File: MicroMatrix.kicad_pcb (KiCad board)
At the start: 2 copper layers, 20 x 20 mm, 70 parts

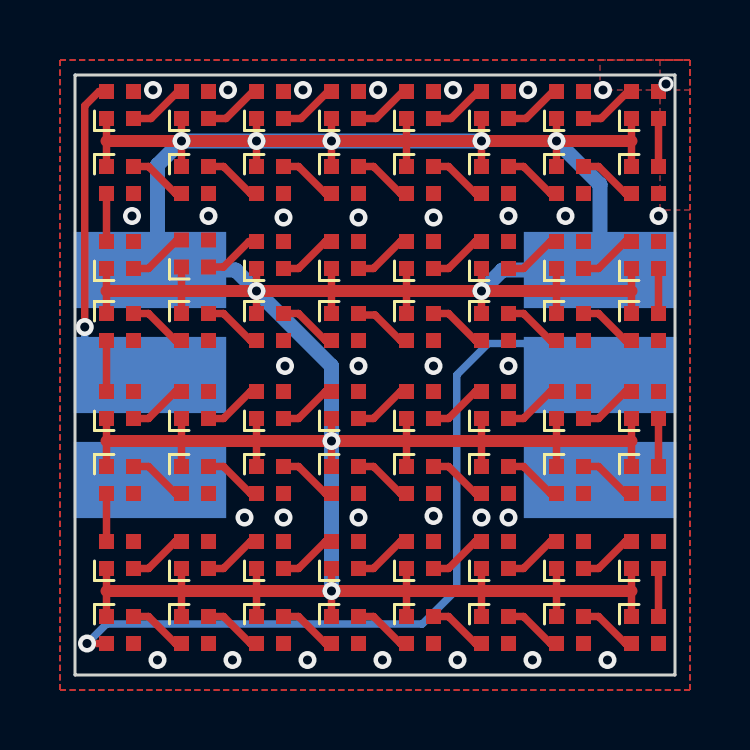
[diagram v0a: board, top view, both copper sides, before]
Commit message: Fixed the 3rd row postion (0.1mm)
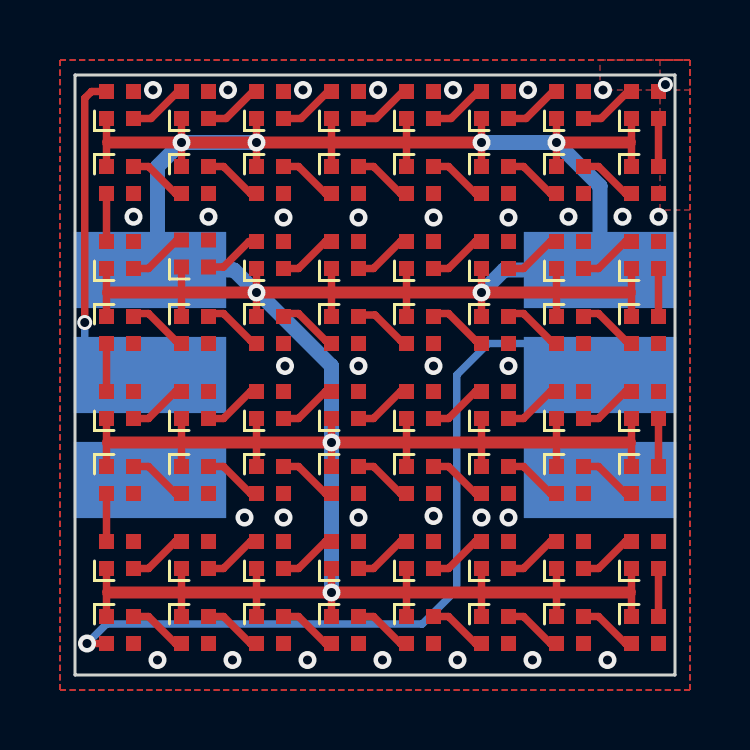
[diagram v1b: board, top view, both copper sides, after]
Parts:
- moved D25 0.10 mm to (149.0, 97.5)
- moved D26 0.10 mm to (146.5, 97.5)
- moved D27 0.10 mm to (144.0, 97.5)
- moved D28 0.10 mm to (141.5, 97.5)
- moved D29 0.10 mm to (139.0, 97.5)
- moved D30 0.10 mm to (136.5, 97.5)
- moved D31 0.10 mm to (134.0, 97.5)
- moved D32 0.10 mm to (131.5, 97.5)
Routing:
- net +5V: track 159.2 -> 151.3 mm, vias 9 -> 8
- net GND: vias 33 -> 34
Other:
- board text added: "REV1.2"
- board text removed: "REV1.1"

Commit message: Updated Panel PCB to REV1.2
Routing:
- net +5V: track 151.3 -> 153.9 mm
- net DIN: track 14.0 -> 15.2 mm
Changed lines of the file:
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@@
   (segment (start 132.533193 90.45) (end 133.433193 89.55) (width 0.25) (layer "F.Cu") (net 1))
   (segment (start 131.95 90.45) (end 132.533193 90.45) (width 0.25) (layer "F.Cu") (net 1))
-  (segment (start 147.6 89.5) (end 147.6 89.4) (width 0.25) (layer "F.Cu") (net 2))
   (via (at 134.45 93.725) (size 0.6) (drill 0.3) (layers "F.Cu" "B.Cu") (free) (net 2))
   (via (at 142.75 108.5) (size 0.6) (drill 0.3) (layers "F.Cu" "B.Cu") (free) (net 2))
@@
   (segment (start 131.05 89.55) (end 130.55 89.55) (width 0.25) (layer "F.Cu") (net 3))
   (via (at 130.325 97.25) (size 0.5) (drill 0.3) (layers "F.Cu" "B.Cu") (free) (net 3))
+  (segment (start 130.325 97.25) (end 130.325 98.075) (width 0.25) (layer "B.Cu") (net 3))
   (segment (start 131.125 99) (end 130.325 98.2) (width 0.25) (layer "B.Cu") (net 3))
+  (segment (start 130.325 98.075) (end 131.75 99.5) (width 0.25) (layer "B.Cu") (net 3))
   (segment (start 132.5 99) (end 130.95 99) (width 0.25) (layer "B.Cu") (net 3))
-  (segment (start 130.325 98.05) (end 130.325 97.25) (width 0.25) (layer "B.Cu") (net 3))
-  (segment (start 130.95 99) (end 130.35 98.4) (width 0.25) (layer "B.Cu") (net 3))
   (segment (start 132.5 99) (end 131.125 99) (width 0.25) (layer "B.Cu") (net 3))
   (segment (start 148.55 101.2) (end 148.55 102.05) (width 0.25) (layer "F.Cu") (net 4))
@@
   (segment (start 143.55 90.45) (end 143.55 92.05) (width 0.25) (layer "F.Cu") (net 4))
   (segment (start 131.05 96.2) (end 131.05 96.95) (width 0.25) (layer "F.Cu") (net 4))
+  (segment (start 131.05 91.25) (end 148.55 91.25) (width 0.4) (layer "F.Cu") (net 4))
   (segment (start 131.05 105.45) (end 131.05 106.2) (width 0.25) (layer "F.Cu") (net 4))
   (segment (start 133.55 107.05) (end 133.55 105.45) (width 0.25) (layer "F.Cu") (net 4))
@@
   (segment (start 131.1 101.25) (end 148.5 101.25) (width 0.4) (layer "F.Cu") (net 4))
   (segment (start 148.55 95.45) (end 148.55 96.2) (width 0.25) (layer "F.Cu") (net 4))
-  (segment (start 146.05 91.25) (end 148.5 91.25) (width 0.4) (layer "F.Cu") (net 4))
   (segment (start 148.55 96.2) (end 148.55 96.95) (width 0.25) (layer "F.Cu") (net 4))
   (segment (start 143.55 96.25) (end 143.55 96.95) (width 0.25) (layer "F.Cu") (net 4))
@@
   (segment (start 148.55 107.05) (end 148.55 106.2) (width 0.25) (layer "F.Cu") (net 4))
   (segment (start 148.55 90.45) (end 148.55 91.2) (width 0.25) (layer "F.Cu") (net 4))
-  (segment (start 131.1 91.25) (end 143.55 91.25) (width 0.4) (layer "F.Cu") (net 4))
   (segment (start 133.55 91.25) (end 133.55 92.05) (width 0.25) (layer "F.Cu") (net 4))
   (segment (start 143.55 105.45) (end 143.55 107.05) (width 0.25) (layer "F.Cu") (net 4))
@@
   (via (at 138.55 106.25) (size 0.6) (drill 0.3) (layers "F.Cu" "B.Cu") (net 4))
   (via (at 146.05 91.25) (size 0.6) (drill 0.3) (layers "F.Cu" "B.Cu") (net 4))
+  (segment (start 146.05 91.25) (end 143.55 91.25) (width 0.5) (layer "B.Cu") (net 4))
   (segment (start 138.55 101.25) (end 138.55 106.25) (width 0.5) (layer "B.Cu") (net 4))
   (segment (start 144.3 95.5) (end 147.5 95.5) (width 0.5) (layer "B.Cu") (net 4))
@@
   (segment (start 133.55 91.25) (end 132.75 92.05) (width 0.5) (layer "B.Cu") (net 4))
   (segment (start 135.3 95.5) (end 132.5 95.5) (width 0.5) (layer "B.Cu") (net 4))
-  (segment (start 143.55 91.25) (end 146.05 91.25) (width 0.5) (layer "B.Cu") (net 4))
   (segment (start 136.05 96.25) (end 135.3 95.5) (width 0.5) (layer "B.Cu") (net 4))
   (segment (start 132.75 95.25) (end 132.5 95.5) (width 0.25) (layer "B.Cu") (net 4))

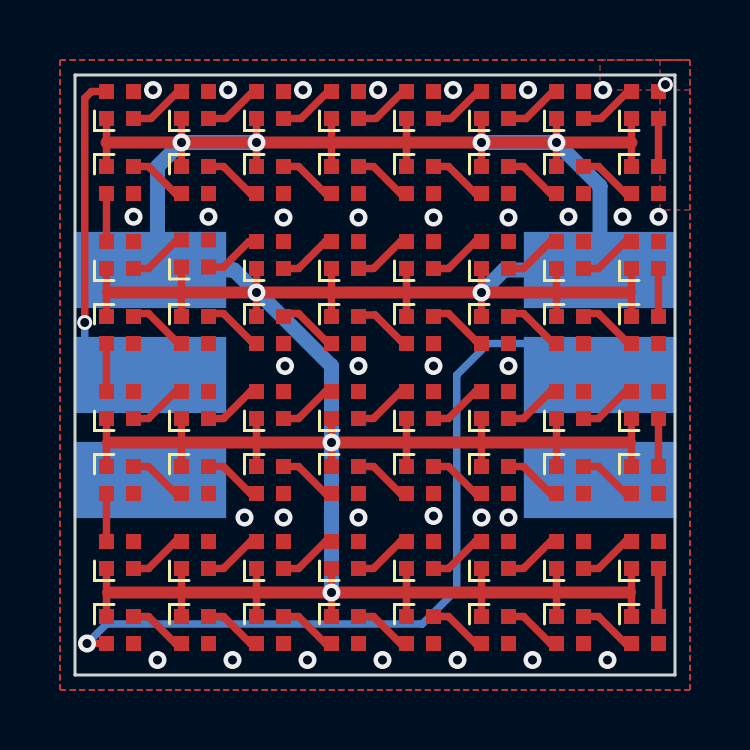
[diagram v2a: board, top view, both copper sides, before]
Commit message: Fixed Trace in REV1.2
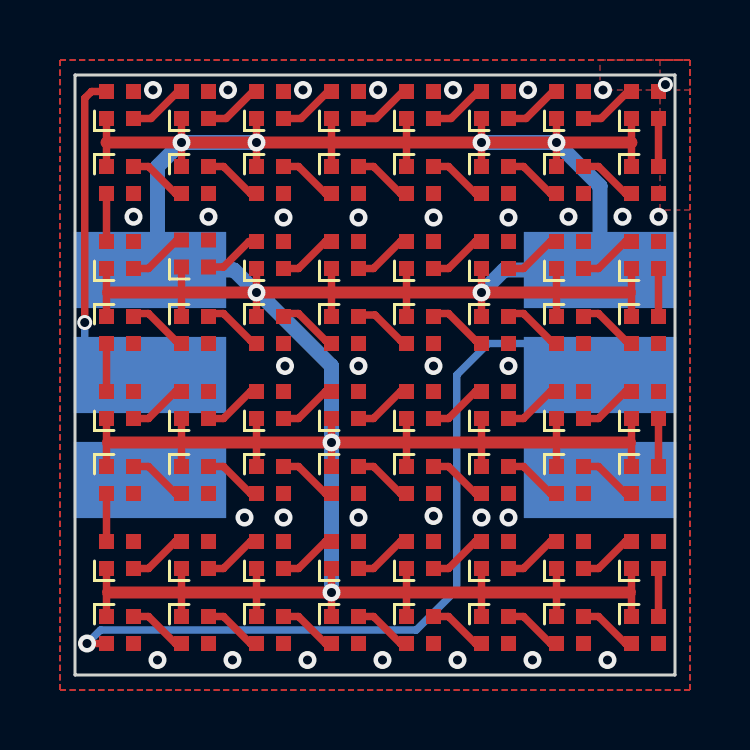
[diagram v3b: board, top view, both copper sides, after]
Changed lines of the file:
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@@
   (segment (start 130.4 107.95) (end 131.05 107.95) (width 0.25) (layer "F.Cu") (net 67))
   (via (at 130.4 107.95) (size 0.6) (drill 0.3) (layers "F.Cu" "B.Cu") (free) (net 67))
+  (segment (start 142.725 99) (end 142.725 106.15) (width 0.25) (layer "B.Cu") (net 67))
   (segment (start 143.775 97.95) (end 142.725 99) (width 0.25) (layer "B.Cu") (net 67))
-  (segment (start 131.05 107.3) (end 130.4 107.95) (width 0.25) (layer "B.Cu") (net 67))
-  (segment (start 142.725 99) (end 142.725 106.15) (width 0.25) (layer "B.Cu") (net 67))
-  (segment (start 141.575 107.3) (end 131.05 107.3) (width 0.25) (layer "B.Cu") (net 67))
-  (segment (start 146.45 97.95) (end 147.5 99) (width 0.25) (layer "B.Cu") (net 67))
-  (segment (start 142.725 106.15) (end 141.575 107.3) (width 0.25) (layer "B.Cu") (net 67))
-  (segment (start 143.775 97.95) (end 146.45 97.95) (width 0.25) (layer "B.Cu") (net 67))
+  (segment (start 130.85 107.5) (end 130.4 107.95) (width 0.25) (layer "B.Cu") (net 67))
+  (segment (start 147.5 99) (end 146.45 97.95) (width 0.25) (layer "B.Cu") (net 67))
+  (segment (start 146.45 97.95) (end 143.775 97.95) (width 0.25) (layer "B.Cu") (net 67))
+  (segment (start 141.375 107.5) (end 130.85 107.5) (width 0.25) (layer "B.Cu") (net 67))
+  (segment (start 142.725 106.15) (end 141.375 107.5) (width 0.25) (layer "B.Cu") (net 67))
   (zone locked (net 2) (net_name "GND") (layers F&B.Cu) (hatch edge 0.508)
     (connect_pads (clearance 0.128))

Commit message: Updated PCB to REV1.3 Replaced SK6805 footprint/symbol with a own version
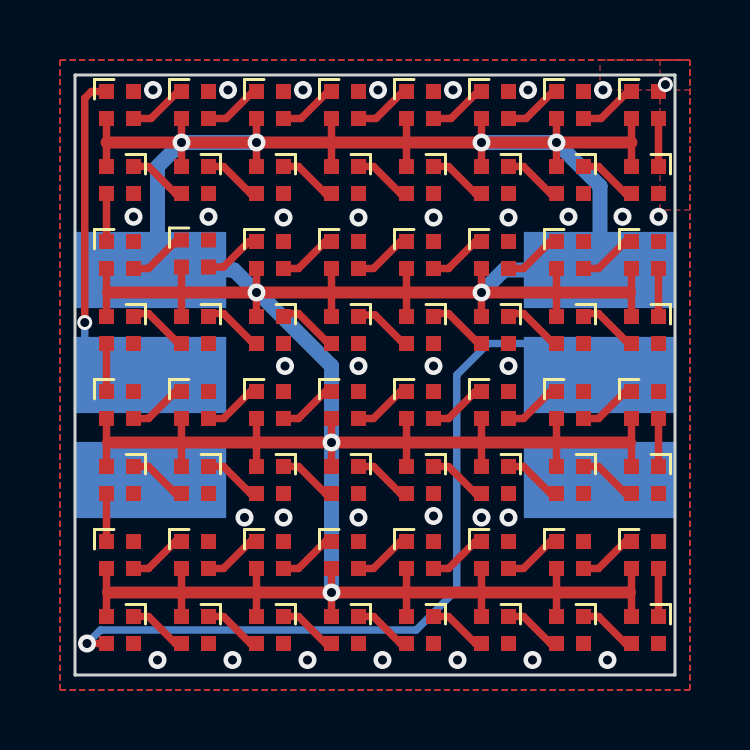
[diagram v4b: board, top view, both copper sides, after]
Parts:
- D1, D10, D11, D12, D13, D14, D15, D16, D17, D18, D19, D2, D20, D21, D22, D23, D24, D25, D26, D27, D28, D29, D3, D30, D31, D32, D33, D34, D35, D36, D37, D38, D39, D4, D40, D41, D42, D43, D44, D45, D46, D47, D48, D49, D5, D50, D51, D52, D53, D54, D55, D56, D57, D58, D59, D6, D60, D61, D62, D63, D64, D7, D8, D9: footprint LED_SMD:LED_SK6812_EC15_1.5x1.5mm -> SK6805-EC15:SK6805-EC15
- turned D1 to 0 degrees
- turned D10 to -90 degrees
- turned D11 to -90 degrees
- turned D12 to -90 degrees
- turned D13 to -90 degrees
- turned D14 to -90 degrees
- turned D15 to -90 degrees
- turned D16 to -90 degrees
- turned D17 to 0 degrees
- turned D18 to 0 degrees
- turned D19 to 0 degrees
- turned D2 to 0 degrees
- turned D20 to 0 degrees
- turned D21 to 0 degrees
- turned D22 to 0 degrees
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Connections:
- D1 pad 1: Net-(D1-Pad1) -> DIN
- D1 pad 2: GND -> +5V
- D1 pad 3: DIN -> Net-(D1-DOUT)
- D1 pad 4: +5V -> GND
- D10 pad 1: Net-(D10-Pad1) -> Net-(D10-DIN)
- D10 pad 2: GND -> +5V
- D10 pad 3: Net-(D10-Pad3) -> Net-(D10-DOUT)
- D10 pad 4: +5V -> GND
- D11 pad 1: Net-(D11-Pad1) -> Net-(D10-DOUT)
- D11 pad 2: GND -> +5V
- D11 pad 3: Net-(D10-Pad1) -> Net-(D11-DOUT)
- D11 pad 4: +5V -> GND
- D12 pad 1: Net-(D12-Pad1) -> Net-(D11-DOUT)
- D12 pad 2: GND -> +5V
- D12 pad 3: Net-(D11-Pad1) -> Net-(D12-DOUT)
- D12 pad 4: +5V -> GND
- D13 pad 1: Net-(D13-Pad1) -> Net-(D12-DOUT)
- D13 pad 2: GND -> +5V
- D13 pad 3: Net-(D12-Pad1) -> Net-(D13-DOUT)
- D13 pad 4: +5V -> GND
- D14 pad 1: Net-(D14-Pad1) -> Net-(D13-DOUT)
- D14 pad 2: GND -> +5V
- D14 pad 3: Net-(D13-Pad1) -> Net-(D14-DOUT)
- D14 pad 4: +5V -> GND
- D15 pad 1: Net-(D15-Pad1) -> Net-(D14-DOUT)
- D15 pad 2: GND -> +5V
- D15 pad 3: Net-(D14-Pad1) -> Net-(D15-DOUT)
- D15 pad 4: +5V -> GND
- D16 pad 1: Net-(D16-Pad1) -> Net-(D15-DOUT)
- D16 pad 2: GND -> +5V
- D16 pad 3: Net-(D15-Pad1) -> Net-(D16-DOUT)
- D16 pad 4: +5V -> GND
- D17 pad 1: Net-(D17-Pad1) -> Net-(D16-DOUT)
- D17 pad 2: GND -> +5V
- D17 pad 3: Net-(D16-Pad1) -> Net-(D17-DOUT)
- D17 pad 4: +5V -> GND
- D18 pad 1: Net-(D18-Pad1) -> Net-(D17-DOUT)
- D18 pad 2: GND -> +5V
- D18 pad 3: Net-(D17-Pad1) -> Net-(D18-DOUT)
- D18 pad 4: +5V -> GND
- D19 pad 1: Net-(D19-Pad1) -> Net-(D18-DOUT)
- D19 pad 2: GND -> +5V
- D19 pad 3: Net-(D18-Pad1) -> Net-(D19-DOUT)
- D19 pad 4: +5V -> GND
- D2 pad 1: Net-(D2-Pad1) -> Net-(D1-DOUT)
- D2 pad 2: GND -> +5V
- D2 pad 3: Net-(D1-Pad1) -> Net-(D2-DOUT)
- D2 pad 4: +5V -> GND
- D20 pad 1: Net-(D20-Pad1) -> Net-(D19-DOUT)
- D20 pad 2: GND -> +5V
- D20 pad 3: Net-(D19-Pad1) -> Net-(D20-DOUT)
- D20 pad 4: +5V -> GND
- D21 pad 1: Net-(D21-Pad1) -> Net-(D20-DOUT)
- D21 pad 2: GND -> +5V
- D21 pad 3: Net-(D20-Pad1) -> Net-(D21-DOUT)
- D21 pad 4: +5V -> GND
- D22 pad 1: Net-(D22-Pad1) -> Net-(D21-DOUT)
- D22 pad 2: GND -> +5V
- D22 pad 3: Net-(D21-Pad1) -> Net-(D22-DOUT)
- D22 pad 4: +5V -> GND
- D23 pad 1: Net-(D23-Pad1) -> Net-(D22-DOUT)
- D23 pad 2: GND -> +5V
- D23 pad 3: Net-(D22-Pad1) -> Net-(D23-DOUT)
- D23 pad 4: +5V -> GND
- D24 pad 1: Net-(D24-Pad1) -> Net-(D23-DOUT)
- D24 pad 2: GND -> +5V
- D24 pad 3: Net-(D23-Pad1) -> Net-(D24-DOUT)
- D24 pad 4: +5V -> GND
- D25 pad 1: Net-(D25-Pad1) -> Net-(D24-DOUT)
- D25 pad 2: GND -> +5V
- D25 pad 3: Net-(D24-Pad1) -> Net-(D25-DOUT)
- D25 pad 4: +5V -> GND
- D26 pad 1: Net-(D26-Pad1) -> Net-(D25-DOUT)
- D26 pad 2: GND -> +5V
- D26 pad 3: Net-(D25-Pad1) -> Net-(D26-DOUT)
- D26 pad 4: +5V -> GND
- D27 pad 1: Net-(D27-Pad1) -> Net-(D26-DOUT)
- D27 pad 2: GND -> +5V
- D27 pad 3: Net-(D26-Pad1) -> Net-(D27-DOUT)
- D27 pad 4: +5V -> GND
- D28 pad 1: Net-(D28-Pad1) -> Net-(D27-DOUT)
- D28 pad 2: GND -> +5V
- D28 pad 3: Net-(D27-Pad1) -> Net-(D28-DOUT)
- D28 pad 4: +5V -> GND
- D29 pad 1: Net-(D29-Pad1) -> Net-(D28-DOUT)
- D29 pad 2: GND -> +5V
- D29 pad 3: Net-(D28-Pad1) -> Net-(D29-DOUT)
- D29 pad 4: +5V -> GND
- D3 pad 1: Net-(D3-Pad1) -> Net-(D2-DOUT)
- D3 pad 2: GND -> +5V
- D3 pad 3: Net-(D2-Pad1) -> Net-(D3-DOUT)
- D3 pad 4: +5V -> GND
- D30 pad 1: Net-(D30-Pad1) -> Net-(D29-DOUT)
- D30 pad 2: GND -> +5V
- D30 pad 3: Net-(D29-Pad1) -> Net-(D30-DOUT)
- D30 pad 4: +5V -> GND
- D31 pad 1: Net-(D31-Pad1) -> Net-(D30-DOUT)
- D31 pad 2: GND -> +5V
- D31 pad 3: Net-(D30-Pad1) -> Net-(D31-DOUT)
- D31 pad 4: +5V -> GND
- D32 pad 1: Net-(D32-Pad1) -> Net-(D31-DOUT)
- D32 pad 2: GND -> +5V
- D32 pad 3: Net-(D31-Pad1) -> Net-(D32-DOUT)
- D32 pad 4: +5V -> GND
- D33 pad 1: Net-(D33-Pad1) -> Net-(D32-DOUT)
- D33 pad 2: GND -> +5V
- D33 pad 3: Net-(D32-Pad1) -> Net-(D33-DOUT)
- D33 pad 4: +5V -> GND
- D34 pad 1: Net-(D34-Pad1) -> Net-(D33-DOUT)
- D34 pad 2: GND -> +5V
- D34 pad 3: Net-(D33-Pad1) -> Net-(D34-DOUT)
- D34 pad 4: +5V -> GND
- D35 pad 1: Net-(D35-Pad1) -> Net-(D34-DOUT)
- D35 pad 2: GND -> +5V
- D35 pad 3: Net-(D34-Pad1) -> Net-(D35-DOUT)
- D35 pad 4: +5V -> GND
- D36 pad 1: Net-(D36-Pad1) -> Net-(D35-DOUT)
- D36 pad 2: GND -> +5V
- D36 pad 3: Net-(D35-Pad1) -> Net-(D36-DOUT)
- D36 pad 4: +5V -> GND
- D37 pad 1: Net-(D37-Pad1) -> Net-(D36-DOUT)
- D37 pad 2: GND -> +5V
- D37 pad 3: Net-(D36-Pad1) -> Net-(D37-DOUT)
- D37 pad 4: +5V -> GND
- D38 pad 1: Net-(D38-Pad1) -> Net-(D37-DOUT)
- D38 pad 2: GND -> +5V
- D38 pad 3: Net-(D37-Pad1) -> Net-(D38-DOUT)
- D38 pad 4: +5V -> GND
- D39 pad 1: Net-(D39-Pad1) -> Net-(D38-DOUT)
- D39 pad 2: GND -> +5V
- D39 pad 3: Net-(D38-Pad1) -> Net-(D39-DOUT)
- D39 pad 4: +5V -> GND
- D4 pad 1: Net-(D4-Pad1) -> Net-(D3-DOUT)
- D4 pad 2: GND -> +5V
- D4 pad 3: Net-(D3-Pad1) -> Net-(D4-DOUT)
- D4 pad 4: +5V -> GND
- D40 pad 1: Net-(D40-Pad1) -> Net-(D39-DOUT)
- D40 pad 2: GND -> +5V
- D40 pad 3: Net-(D39-Pad1) -> Net-(D40-DOUT)
- D40 pad 4: +5V -> GND
- D41 pad 1: Net-(D41-Pad1) -> Net-(D40-DOUT)
- D41 pad 2: GND -> +5V
- D41 pad 3: Net-(D40-Pad1) -> Net-(D41-DOUT)
- D41 pad 4: +5V -> GND
- D42 pad 1: Net-(D42-Pad1) -> Net-(D41-DOUT)
- D42 pad 2: GND -> +5V
- D42 pad 3: Net-(D41-Pad1) -> Net-(D42-DOUT)
- D42 pad 4: +5V -> GND
- D43 pad 1: Net-(D43-Pad1) -> Net-(D42-DOUT)
- D43 pad 2: GND -> +5V
- D43 pad 3: Net-(D42-Pad1) -> Net-(D43-DOUT)
- D43 pad 4: +5V -> GND
- D44 pad 1: Net-(D44-Pad1) -> Net-(D43-DOUT)
- D44 pad 2: GND -> +5V
- D44 pad 3: Net-(D43-Pad1) -> Net-(D44-DOUT)
- D44 pad 4: +5V -> GND
- D45 pad 1: Net-(D45-Pad1) -> Net-(D44-DOUT)
- D45 pad 2: GND -> +5V
- D45 pad 3: Net-(D44-Pad1) -> Net-(D45-DOUT)
- D45 pad 4: +5V -> GND
- D46 pad 1: Net-(D46-Pad1) -> Net-(D45-DOUT)
- D46 pad 2: GND -> +5V
- D46 pad 3: Net-(D45-Pad1) -> Net-(D46-DOUT)
- D46 pad 4: +5V -> GND
- D47 pad 1: Net-(D47-Pad1) -> Net-(D46-DOUT)
- D47 pad 2: GND -> +5V
- D47 pad 3: Net-(D46-Pad1) -> Net-(D47-DOUT)
- D47 pad 4: +5V -> GND
- D48 pad 1: Net-(D48-Pad1) -> Net-(D47-DOUT)
- D48 pad 2: GND -> +5V
- D48 pad 3: Net-(D47-Pad1) -> Net-(D48-DOUT)
- D48 pad 4: +5V -> GND
- D49 pad 1: Net-(D49-Pad1) -> Net-(D48-DOUT)
- D49 pad 2: GND -> +5V
- D49 pad 3: Net-(D48-Pad1) -> Net-(D49-DOUT)
- D49 pad 4: +5V -> GND
- D5 pad 1: Net-(D5-Pad1) -> Net-(D4-DOUT)
- D5 pad 2: GND -> +5V
- D5 pad 3: Net-(D4-Pad1) -> Net-(D5-DOUT)
- D5 pad 4: +5V -> GND
- D50 pad 1: Net-(D50-Pad1) -> Net-(D49-DOUT)
- D50 pad 2: GND -> +5V
- D50 pad 3: Net-(D49-Pad1) -> Net-(D50-DOUT)
- D50 pad 4: +5V -> GND
- D51 pad 1: Net-(D51-Pad1) -> Net-(D50-DOUT)
- D51 pad 2: GND -> +5V
- D51 pad 3: Net-(D50-Pad1) -> Net-(D51-DOUT)
- D51 pad 4: +5V -> GND
- D52 pad 1: Net-(D52-Pad1) -> Net-(D51-DOUT)
- D52 pad 2: GND -> +5V
- D52 pad 3: Net-(D51-Pad1) -> Net-(D52-DOUT)
- D52 pad 4: +5V -> GND
- D53 pad 1: Net-(D53-Pad1) -> Net-(D52-DOUT)
- D53 pad 2: GND -> +5V
- D53 pad 3: Net-(D52-Pad1) -> Net-(D53-DOUT)
- D53 pad 4: +5V -> GND
- D54 pad 1: Net-(D54-Pad1) -> Net-(D53-DOUT)
- D54 pad 2: GND -> +5V
- D54 pad 3: Net-(D53-Pad1) -> Net-(D54-DOUT)
- D54 pad 4: +5V -> GND
- D55 pad 1: Net-(D55-Pad1) -> Net-(D54-DOUT)
- D55 pad 2: GND -> +5V
- D55 pad 3: Net-(D54-Pad1) -> Net-(D55-DOUT)
- D55 pad 4: +5V -> GND
- D56 pad 1: Net-(D56-Pad1) -> Net-(D55-DOUT)
- D56 pad 2: GND -> +5V
- D56 pad 3: Net-(D55-Pad1) -> Net-(D56-DOUT)
- D56 pad 4: +5V -> GND
- D57 pad 1: Net-(D57-Pad1) -> Net-(D56-DOUT)
- D57 pad 2: GND -> +5V
- D57 pad 3: Net-(D56-Pad1) -> Net-(D57-DOUT)
- D57 pad 4: +5V -> GND
- D58 pad 1: Net-(D58-Pad1) -> Net-(D57-DOUT)
- D58 pad 2: GND -> +5V
- D58 pad 3: Net-(D57-Pad1) -> Net-(D58-DOUT)
- D58 pad 4: +5V -> GND
- D59 pad 1: Net-(D59-Pad1) -> Net-(D58-DOUT)
- D59 pad 2: GND -> +5V
- D59 pad 3: Net-(D58-Pad1) -> Net-(D59-DOUT)
- D59 pad 4: +5V -> GND
- D6 pad 1: Net-(D6-Pad1) -> Net-(D5-DOUT)
- D6 pad 2: GND -> +5V
- D6 pad 3: Net-(D5-Pad1) -> Net-(D6-DOUT)
- D6 pad 4: +5V -> GND
- D60 pad 1: Net-(D60-Pad1) -> Net-(D59-DOUT)
- D60 pad 2: GND -> +5V
- D60 pad 3: Net-(D59-Pad1) -> Net-(D60-DOUT)
- D60 pad 4: +5V -> GND
- D61 pad 1: Net-(D61-Pad1) -> Net-(D60-DOUT)
- D61 pad 2: GND -> +5V
- D61 pad 3: Net-(D60-Pad1) -> Net-(D61-DOUT)
- D61 pad 4: +5V -> GND
- D62 pad 1: Net-(D62-Pad1) -> Net-(D61-DOUT)
- D62 pad 2: GND -> +5V
- D62 pad 3: Net-(D61-Pad1) -> Net-(D62-DOUT)
- D62 pad 4: +5V -> GND
- D63 pad 1: Net-(D63-Pad1) -> Net-(D62-DOUT)
- D63 pad 2: GND -> +5V
- D63 pad 3: Net-(D62-Pad1) -> Net-(D63-DOUT)
- D63 pad 4: +5V -> GND
- D64 pad 1: DOUT -> Net-(D63-DOUT)
- D64 pad 2: GND -> +5V
- D64 pad 3: Net-(D63-Pad1) -> DOUT
- D64 pad 4: +5V -> GND
- D7 pad 1: Net-(D7-Pad1) -> Net-(D6-DOUT)
- D7 pad 2: GND -> +5V
- D7 pad 3: Net-(D6-Pad1) -> Net-(D7-DOUT)
- D7 pad 4: +5V -> GND
- D8 pad 1: Net-(D8-Pad1) -> Net-(D7-DOUT)
- D8 pad 2: GND -> +5V
- D8 pad 3: Net-(D7-Pad1) -> Net-(D8-DOUT)
- D8 pad 4: +5V -> GND
- D9 pad 1: Net-(D10-Pad3) -> Net-(D8-DOUT)
- D9 pad 2: GND -> +5V
- D9 pad 3: Net-(D8-Pad1) -> Net-(D10-DIN)
- D9 pad 4: +5V -> GND
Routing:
- net Net-(D54-Pad1): track 2.07 -> 0.00 mm
- net Net-(D54-DOUT): track 0.00 -> 2.07 mm
- net Net-(D17-Pad1): track 1.99 -> 0.00 mm
- net Net-(D17-DOUT): track 0.00 -> 1.99 mm
- net Net-(D7-Pad1): track 1.97 -> 0.00 mm
- net Net-(D7-DOUT): track 0.00 -> 1.97 mm
- net Net-(D6-Pad1): track 1.97 -> 0.00 mm
- net Net-(D6-DOUT): track 0.00 -> 1.97 mm
- net Net-(D5-Pad1): track 1.97 -> 0.00 mm
- net Net-(D5-DOUT): track 0.00 -> 1.97 mm
- net Net-(D4-Pad1): track 1.97 -> 0.00 mm
- net Net-(D4-DOUT): track 0.00 -> 1.97 mm
- net Net-(D3-Pad1): track 1.97 -> 0.00 mm
- net Net-(D3-DOUT): track 0.00 -> 1.97 mm
- net Net-(D2-Pad1): track 1.97 -> 0.00 mm
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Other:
- board text added: "2024/01"
- board text added: "REV1.3"
- board text removed: "2022/06"
- board text removed: "REV1.2"
